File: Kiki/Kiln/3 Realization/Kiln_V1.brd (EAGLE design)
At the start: 68.6 x 53.3 mm, 24 parts, among them Q1 2N3904, Q2 2N3904, Q3 2N3904, Q4 2N3904, X1 3.5mm term

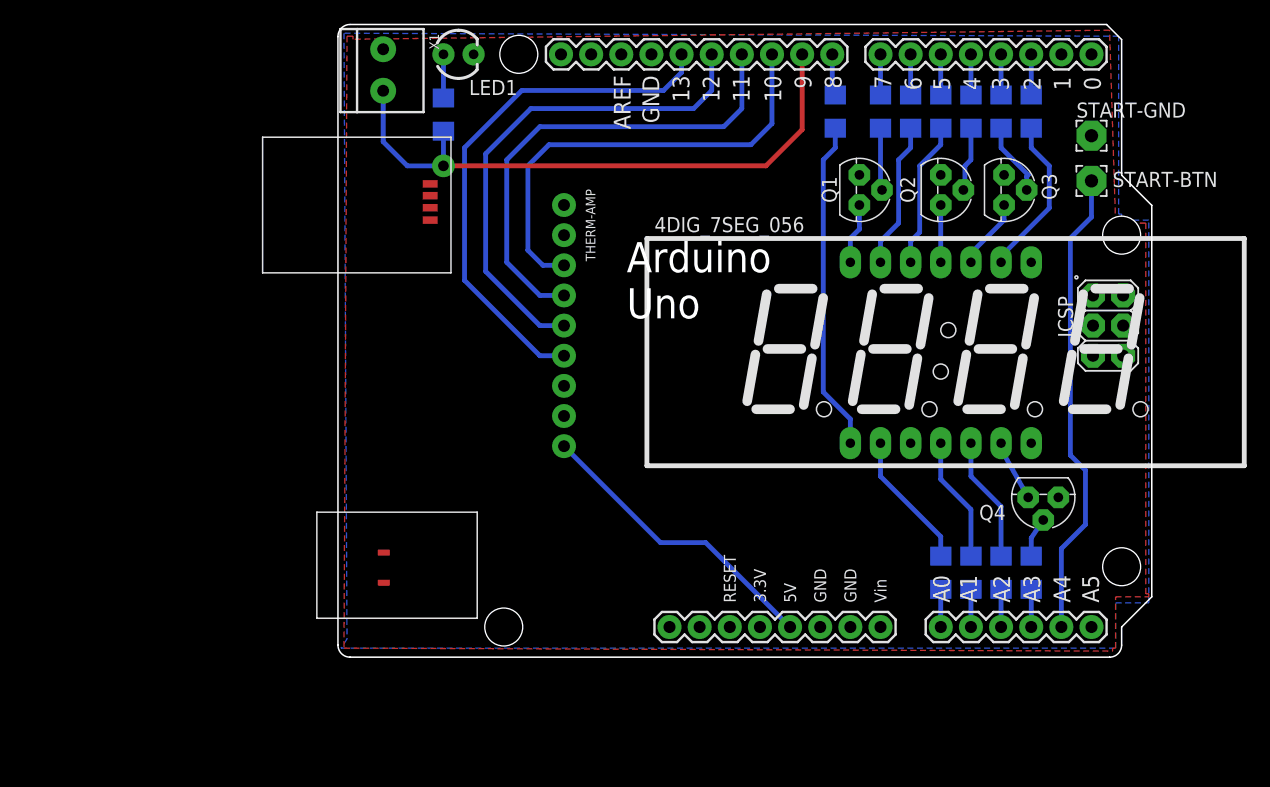
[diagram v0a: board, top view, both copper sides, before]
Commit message: Update: final comments Fixed all the things listed in the final comments
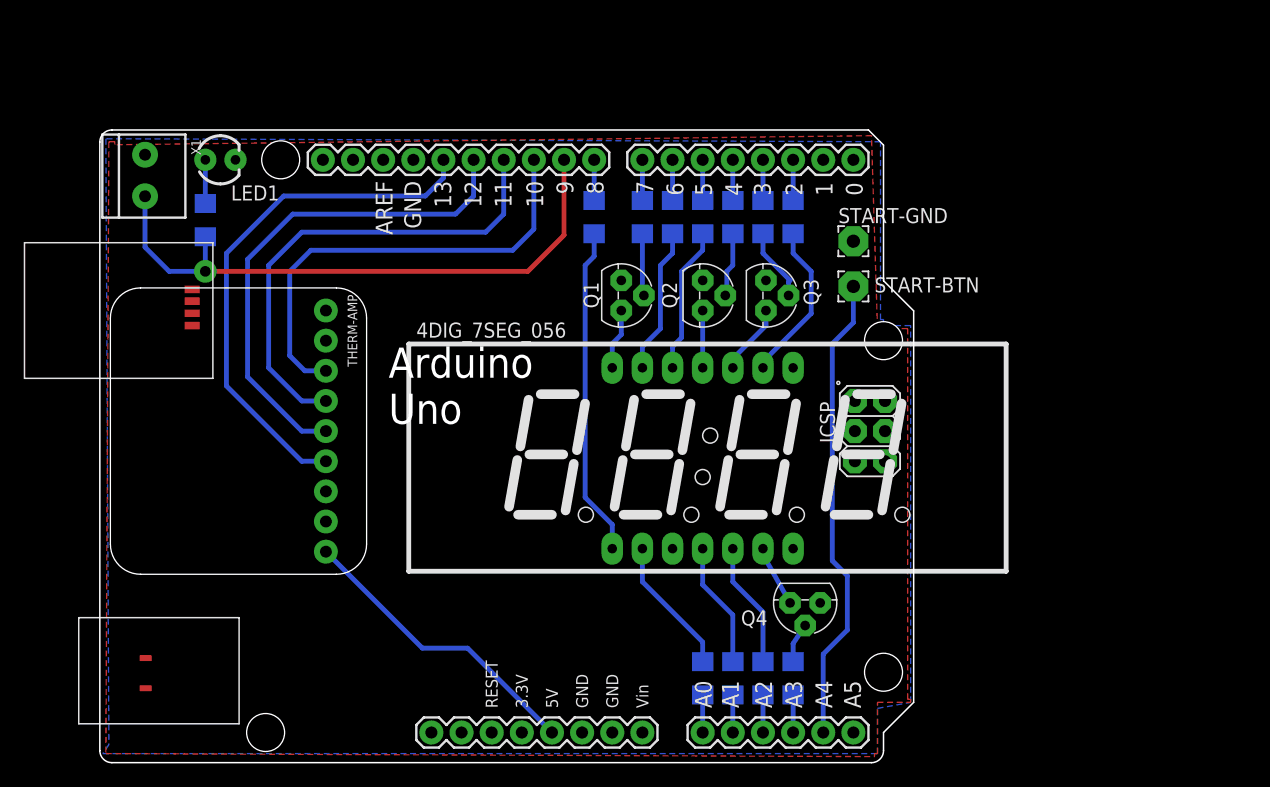
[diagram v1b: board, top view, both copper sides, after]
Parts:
- moved R4 22.2 mm to (41.9, 46.0)
- moved R11 21.9 mm to (46.0, 46.0)
- moved 4DIG_7SEG_056 21.9 mm to (51.1, 25.7)
- moved LED1 21.9 mm to (10.4, 50.8)
- moved Q1 21.9 mm to (44.2, 39.4)
- moved Q2 21.9 mm to (51.1, 39.4)
- moved Q4 21.9 mm to (59.7, 13.5)
- moved R12 21.9 mm to (9.14, 45.7)
- moved R2 21.9 mm to (51.1, 46.0)
- moved R5 21.9 mm to (51.1, 7.11)
- moved R7 21.9 mm to (56.1, 7.11)
- moved R9 21.9 mm to (56.1, 46.0)
- moved PCB1 21.9 mm to (0.25, 0.00)
- moved THERM-AMP 21.9 mm to (19.3, 27.9)
- moved X1 21.9 mm to (4.06, 49.5)
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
